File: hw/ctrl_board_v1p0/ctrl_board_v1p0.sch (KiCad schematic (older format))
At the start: 31 parts, among them J1 RaSCSI Connector, J2 OLED Connector, P1 Conn_02x20_Odd_Even, SW1 SW_SPST, SW2 SW_SPST, SW3 SW_SPST, SW4 Rotary_Encoder_Switch, U1 PCA9554APW,118

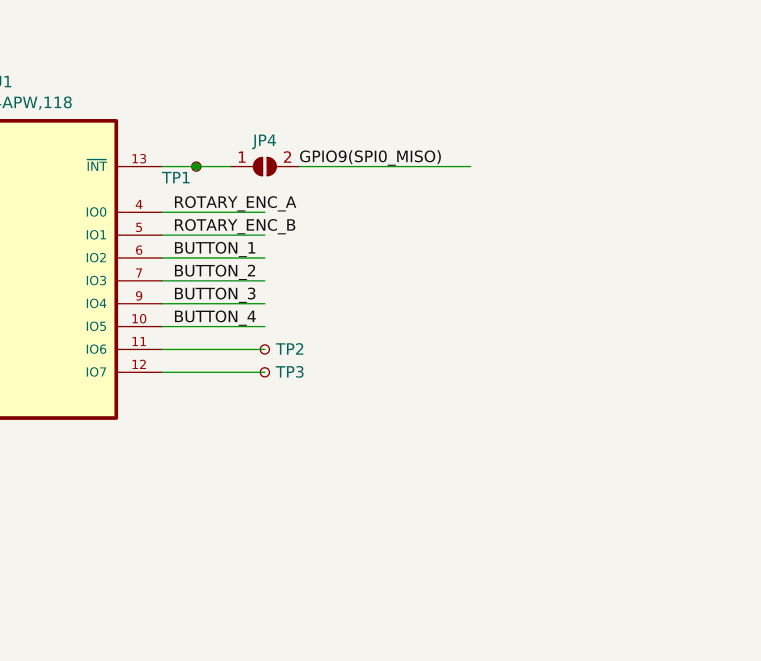
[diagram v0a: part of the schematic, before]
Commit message: routed signals
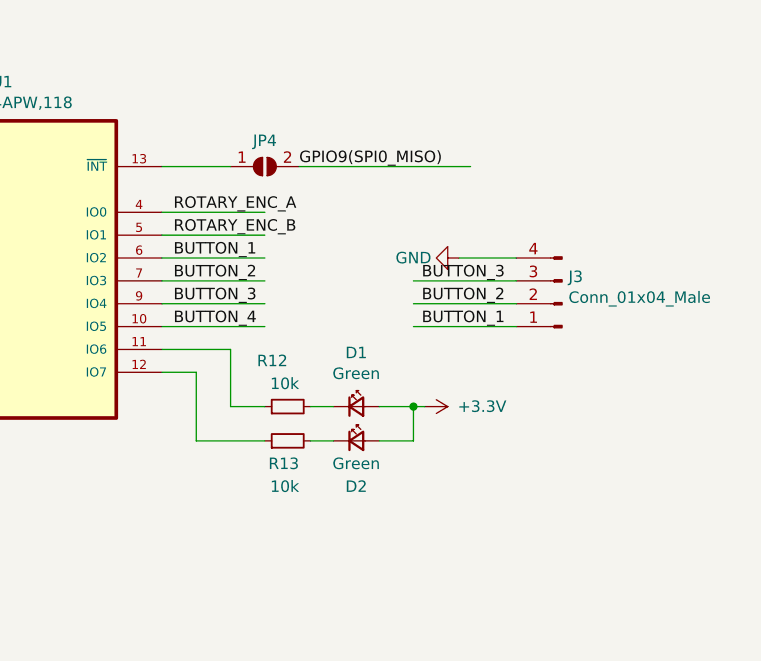
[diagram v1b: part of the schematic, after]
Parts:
- removed TP1, TP2, TP3: TestPoint_Small, TestPoint:TestPoint_Pad_D1.0mm, symbol Connector:TestPoint_Small
- added D1, D2: Green, LED_SMD:LED_0805_2012Metric, symbol Device:LED_Small
- added J3: Conn_01x04_Male, Connector_PinHeader_2.54mm:PinHeader_1x04_P2.54mm_Vertical, symbol Connector:Conn_01x04_Male
- added R12, R13: 10k, Resistor_SMD:R_0805_2012Metric, symbol Device:R_Small
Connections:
- wire segments 136 -> 149
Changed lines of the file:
@@
 Wire Wire Line
 	6550 3200 7050 3200
-$Comp
-L Connector:TestPoint_Small TP1
-U 1 1 61C8D834
-P 8600 2900
-F 0 "TP1" H 8450 2850 50  0000 L CNN
-F 1 "TestPoint_Small" H 8648 2855 50  0001 L CNN
-F 2 "TestPoint:TestPoint_Pad_D1.0mm" H 8800 2900 50  0001 C CNN
-F 3 "~" H 8800 2900 50  0001 C CNN
-	1    8600 2900
-	1    0    0    -1
-$EndComp
-$Comp
-L Connector:TestPoint_Small TP2
-U 1 1 61C8D83A
-P 8900 3700
-F 0 "TP2" H 8948 3700 50  0000 L CNN
-F 1 "TestPoint_Small" H 8948 3655 50  0001 L CNN
-F 2 "TestPoint:TestPoint_Pad_D1.0mm" H 9100 3700 50  0001 C CNN
-F 3 "~" H 9100 3700 50  0001 C CNN
-	1    8900 3700
-	1    0    0    -1
-$EndComp
-$Comp
-L Connector:TestPoint_Small TP3
-U 1 1 61C8D840
-P 8900 3800
-F 0 "TP3" H 8948 3800 50  0000 L CNN
-F 1 "TestPoint_Small" H 8948 3755 50  0001 L CNN
-F 2 "TestPoint:TestPoint_Pad_D1.0mm" H 9100 3800 50  0001 C CNN
-F 3 "~" H 9100 3800 50  0001 C CNN
-	1    8900 3800
-	1    0    0    -1
-$EndComp
 Text Label 8500 3300 0    50   ~ 0
 BUTTON_1
@@
 BUTTON_4
 Wire Wire Line
-	8450 3800 8900 3800
-Wire Wire Line
-	8450 3700 8900 3700
-Wire Wire Line
 	8450 3600 8900 3600
 Wire Wire Line
@@
 	1    0    0    -1
 $EndComp
-Wire Wire Line
-	8450 2900 8600 2900
-Connection ~ 8600 2900
-Wire Wire Line
-	8600 2900 8750 2900
 Wire Wire Line
 	1250 2100 2400 2100
@@
 Wire Wire Line
 	6550 2900 6550 2850
+Wire Wire Line
+	8450 2900 8750 2900
+$Comp
+L Connector:Conn_01x04_Male J3
+U 1 1 61B9A469
+P 10200 3500
+F 0 "J3" H 10172 3382 50  0000 R CNN
+F 1 "Conn_01x04_Male" H 10172 3473 50  0000 R CNN
+F 2 "Connector_PinHeader_2.54mm:PinHeader_1x04_P2.54mm_Vertical" H 10200 3500 50  0001 C CNN
+F 3 "~" H 10200 3500 50  0001 C CNN
+	1    10200 3500
+	-1   0    0    1
+$EndComp
+Text Label 9950 3600 2    50   ~ 0
+BUTTON_1
+Text Label 9950 3500 2    50   ~ 0
+BUTTON_2
+Text Label 9950 3400 2    50   ~ 0
+BUTTON_3
+Wire Wire Line
+	10000 3400 9550 3400
+Wire Wire Line
+	10000 3500 9550 3500
+Wire Wire Line
+	10000 3600 9550 3600
+$Comp
+L power:GND #PWR032
+U 1 1 61BA62FA
+P 9750 3300
+F 0 "#PWR032" H 9750 3050 50  0001 C CNN
+F 1 "GND" V 9750 3100 50  0000 C CNN
+F 2 "" H 9750 3300 50  0000 C CNN
+F 3 "" H 9750 3300 50  0000 C CNN
+	1    9750 3300
+	0    1    1    0
+$EndComp
+Wire Wire Line
+	10000 3300 9750 3300
+$Comp
+L Device:R_Small R13
+U 1 1 61BB2381
+P 9000 4100
+F 0 "R13" V 8900 4050 50  0000 L CNN
+F 1 "10k" V 8800 4050 50  0000 L CNN
+F 2 "Resistor_SMD:R_0805_2012Metric" H 9000 4100 50  0001 C CNN
+F 3 "~" H 9000 4100 50  0001 C CNN
+F 4 "C17414" H 9000 4100 50  0001 C CNN "LCSC"
+	1    9000 4100
+	0    -1   -1   0
+$EndComp
+$Comp
+L Device:R_Small R12
+U 1 1 61BB79CE
+P 9000 3950
+F 0 "R12" V 9200 3950 50  0000 L CNN
+F 1 "10k" V 9100 3900 50  0000 L CNN
+F 2 "Resistor_SMD:R_0805_2012Metric" H 9000 3950 50  0001 C CNN
+F 3 "~" H 9000 3950 50  0001 C CNN
+F 4 "C17414" H 9000 3950 50  0001 C CNN "LCSC"
+	1    9000 3950
+	0    -1   -1   0
+$EndComp
+$Comp
+L Device:LED_Small D1
+U 1 1 61BBD9AF
+P 9300 3950
+F 0 "D1" H 9300 4185 50  0000 C CNN
+F 1 "Green" H 9300 4094 50  0000 C CNN
+F 2 "LED_SMD:LED_0805_2012Metric" V 9300 3950 50  0001 C CNN
+F 3 "~" V 9300 3950 50  0001 C CNN
+F 4 "C2297" H 9300 3950 50  0001 C CNN "LCSC"
+	1    9300 3950
+	1    0    0    -1
+$EndComp
+$Comp
+L Device:LED_Small D2
+U 1 1 61BBEAAE
+P 9300 4100
+F 0 "D2" H 9300 3900 50  0000 C CNN
+F 1 "Green" H 9300 4000 50  0000 C CNN
+F 2 "LED_SMD:LED_0805_2012Metric" V 9300 4100 50  0001 C CNN
+F 3 "~" V 9300 4100 50  0001 C CNN
+F 4 "C2297" H 9300 4100 50  0001 C CNN "LCSC"
+	1    9300 4100
+	1    0    0    -1
+$EndComp
+Wire Wire Line
+	8450 3700 8750 3700
+Wire Wire Line
+	8750 3700 8750 3950
+Wire Wire Line
+	8750 3950 8900 3950
+Wire Wire Line
+	8900 4100 8600 4100
+Wire Wire Line
+	8600 4100 8600 3800
+Wire Wire Line
+	8600 3800 8450 3800
+Wire Wire Line
+	9100 3950 9200 3950
+Wire Wire Line
+	9200 4100 9100 4100
+$Comp
+L power:+3.3V #PWR031
+U 1 1 61BF0BCF
+P 9600 3950
+F 0 "#PWR031" H 9600 3800 50  0001 C CNN
+F 1 "+3.3V" V 9600 4200 50  0000 C CNN
+F 2 "" H 9600 3950 50  0000 C CNN
+F 3 "" H 9600 3950 50  0000 C CNN
+	1    9600 3950
+	0    1    1    0
+$EndComp
+Wire Wire Line
+	9400 3950 9550 3950
+Wire Wire Line
+	9400 4100 9550 4100
+Wire Wire Line
+	9550 4100 9550 3950
+Connection ~ 9550 3950
+Wire Wire Line
+	9550 3950 9600 3950
 $EndSCHEMATC

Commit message: cleaned up layout
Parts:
- removed D1, D2: Green, LED_SMD:LED_0805_2012Metric, symbol Device:LED_Small
- removed J3: Conn_01x04_Male, Connector_PinHeader_2.54mm:PinHeader_1x04_P2.54mm_Vertical, symbol Connector:Conn_01x04_Male
- added J3: Conn_02x06_Odd_Even, Connector_PinHeader_2.54mm:PinHeader_2x06_P2.54mm_Vertical, symbol Connector_Generic:Conn_02x06_Odd_Even
- J2: footprint Connector_PinSocket_2.54mm:PinSocket_1x04_P2.54mm_Vertical -> mousebites:OLED_Footprint
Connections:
- net labels added: LED_1, LED_2
- wire segments 149 -> 151
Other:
- moved on the sheet: C1, J2, JP1, JP2, JP3, JP4, R12, R13, R7, R8, R9, U1
